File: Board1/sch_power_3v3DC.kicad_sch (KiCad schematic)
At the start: 6 parts, among them U2 TLV76133DCY

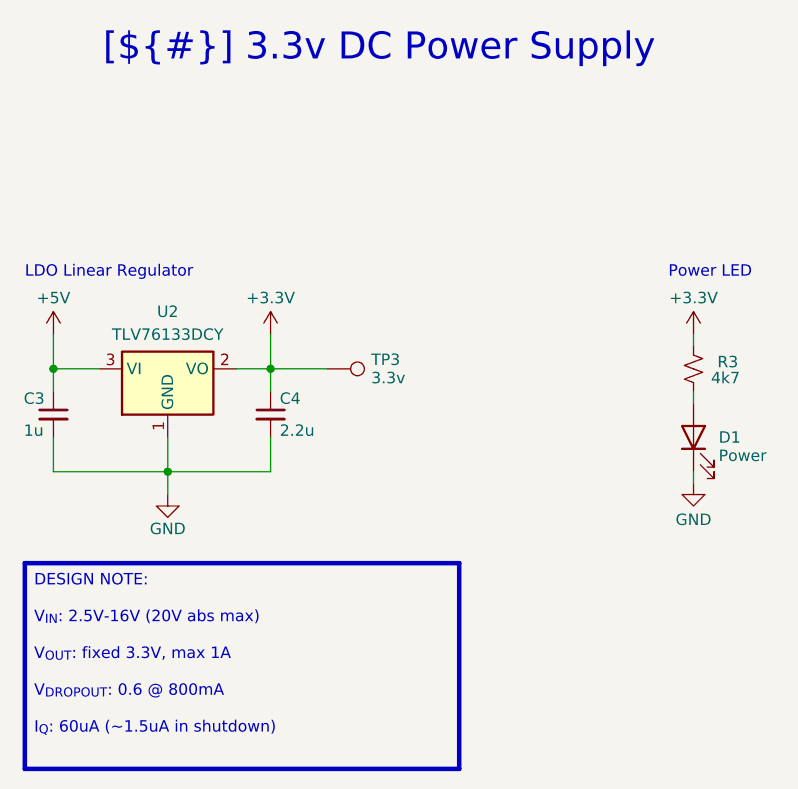
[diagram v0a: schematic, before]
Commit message: Resolve library and ERC issues
No changes to design.
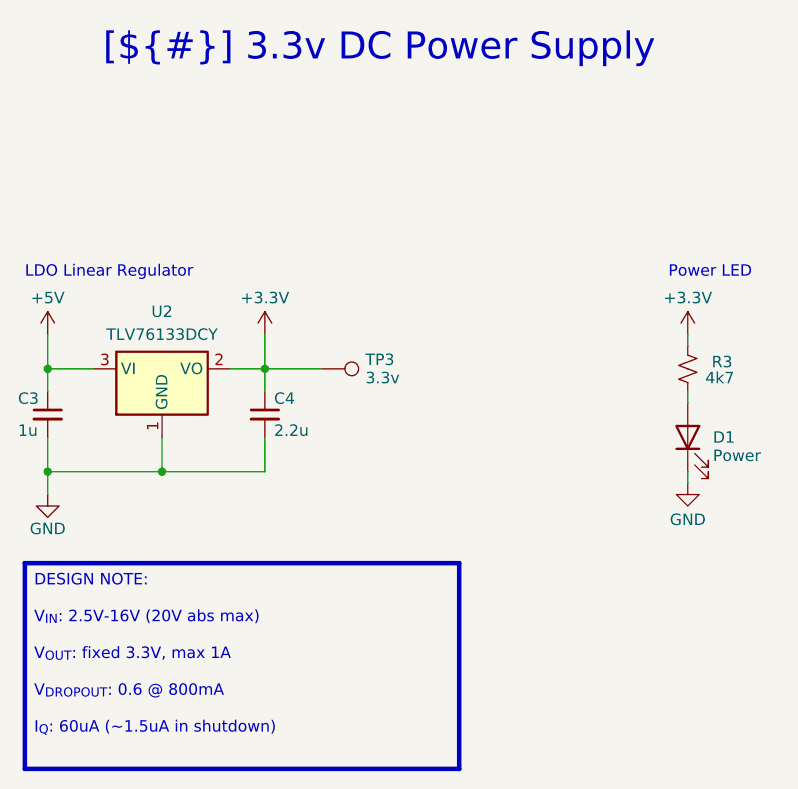
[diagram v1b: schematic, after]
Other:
- moved on the sheet: C3, C4, D1, R3, TP3, U2

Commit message: v1.2 release of board with bug fixes etc
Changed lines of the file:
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@@
 (kicad_sch
-	(version 20231120)
+	(version 20250114)
 	(generator "eeschema")
-	(generator_version "8.0")
+	(generator_version "9.0")
 	(paper "A4")
 	(title_block
 		(title "3.3v DC Power Supply")
-		(date "2025-02-19")
-		(rev "1.1")
+		(date "2025-03-08")
+		(rev "1.2")
 		(company "Wattle Labs")
 	)
-	(junction
-		(at 124.46 66.04)
-		(diameter 0)
-		(color 0 0 0 0)
-	)
-	(junction
-		(at 135.89 54.61)
-		(diameter 0)
-		(color 0 0 0 0)
-	)
-	(junction
-		(at 111.76 54.61)
-		(diameter 0)
-		(color 0 0 0 0)
-	)
-	(junction
-		(at 111.76 66.04)
-		(diameter 0)
-		(color 0 0 0 0)
-	)
-	(wire
-		(pts
-			(xy 124.46 66.04) (xy 135.89 66.04)
-		)
-		(stroke
-			(width 0)
-			(type default)
-		)
-	)
-	(wire
-		(pts
-			(xy 182.88 57.15) (xy 182.88 58.42)
-		)
-		(stroke
-			(width 0)
-			(type default)
-		)
-	)
-	(wire
-		(pts
-			(xy 124.46 66.04) (xy 124.46 62.23)
-		)
-		(stroke
-			(width 0)
-			(type default)
-		)
-	)
-	(wire
-		(pts
-			(xy 135.89 54.61) (xy 132.08 54.61)
-		)
-		(stroke
-			(width 0)
-			(type default)
-		)
-	)
-	(wire
-		(pts
-			(xy 111.76 50.8) (xy 111.76 54.61)
-		)
-		(stroke
-			(width 0)
-			(type default)
-		)
-	)
-	(wire
-		(pts
-			(xy 135.89 54.61) (xy 135.89 57.15)
-		)
-		(stroke
-			(width 0)
-			(type default)
-		)
-	)
-	(wire
-		(pts
-			(xy 182.88 50.8) (xy 182.88 52.07)
-		)
-		(stroke
-			(width 0)
-			(type default)
-		)
-	)
-	(wire
-		(pts
-			(xy 135.89 62.23) (xy 135.89 66.04)
-		)
-		(stroke
-			(width 0)
-			(type default)
-		)
-	)
-	(wire
-		(pts
-			(xy 111.76 54.61) (xy 116.84 54.61)
-		)
-		(stroke
-			(width 0)
-			(type default)
-		)
-	)
-	(wire
-		(pts
-			(xy 135.89 54.61) (xy 142.24 54.61)
-		)
-		(stroke
-			(width 0)
-			(type default)
-		)
-	)
-	(wire
-		(pts
-			(xy 111.76 66.04) (xy 124.46 66.04)
-		)
-		(stroke
-			(width 0)
-			(type default)
-		)
-	)
-	(wire
-		(pts
-			(xy 182.88 66.04) (xy 182.88 67.31)
-		)
-		(stroke
-			(width 0)
-			(type default)
-		)
-	)
-	(wire
-		(pts
-			(xy 135.89 50.8) (xy 135.89 54.61)
-		)
-		(stroke
-			(width 0)
-			(type default)
-		)
-	)
-	(wire
-		(pts
-			(xy 111.76 62.23) (xy 111.76 66.04)
-		)
-		(stroke
-			(width 0)
-			(type default)
-		)
-	)
-	(wire
-		(pts
-			(xy 111.76 66.04) (xy 111.76 68.58)
-		)
-		(stroke
-			(width 0)
-			(type default)
-		)
-	)
-	(wire
-		(pts
-			(xy 111.76 54.61) (xy 111.76 57.15)
-		)
-		(stroke
-			(width 0)
-			(type default)
+	(text "LDO Linear Regulator"
+		(exclude_from_sim no)
+		(at 109.22 43.18 0)
+		(effects
+			(font
+				(size 1.27 1.27)
+				(thickness 0.1588)
+			)
+			(justify left top)
+		)
+	)
+	(text "Power LED"
+		(exclude_from_sim no)
+		(at 180.721 43.18 0)
+		(effects
+			(font
+				(size 1.27 1.27)
+				(thickness 0.1588)
+			)
+			(justify left top)
 		)
 	)
@@
 		(at 109.22 76.2 0)
 		(size 48.26 22.86)
+		(margins 1.2025 1.2025 1.2025 1.2025)
 		(stroke
 			(width 0.5)
@@
 		(at 12.065 12.065 0)
 		(size 273.05 13.335)
+		(margins 2.2499 2.2499 2.2499 2.2499)
 		(stroke
 			(width -0.0001)
@@
 		)
 	)
-	(text "LDO Linear Regulator"
-		(exclude_from_sim no)
-		(at 109.22 43.18 0)
-		(effects
-			(font
-				(size 1.27 1.27)
-				(thickness 0.1588)
-			)
-			(justify left top)
-		)
-	)
-	(text "Power LED"
-		(exclude_from_sim no)
-		(at 180.721 43.18 0)
-		(effects
-			(font
-				(size 1.27 1.27)
-				(thickness 0.1588)
-			)
-			(justify left top)
-		)
-	)
+	(junction
+		(at 124.46 66.04)
+		(diameter 0)
+		(color 0 0 0 0)
+	)
+	(junction
+		(at 135.89 54.61)
+		(diameter 0)
+		(color 0 0 0 0)
+	)
+	(junction
+		(at 111.76 54.61)
+		(diameter 0)
+		(color 0 0 0 0)
+	)
+	(junction
+		(at 111.76 66.04)
+		(diameter 0)
+		(color 0 0 0 0)
+	)
+	(wire
+		(pts
+			(xy 124.46 66.04) (xy 135.89 66.04)
+		)
+		(stroke
+			(width 0)
+			(type default)
+		)
+	)
+	(wire
+		(pts
+			(xy 182.88 57.15) (xy 182.88 58.42)
+		)
+		(stroke
+			(width 0)
+			(type default)
+		)
+	)
+	(wire
+		(pts
+			(xy 124.46 66.04) (xy 124.46 62.23)
+		)
+		(stroke
+			(width 0)
+			(type default)
+		)
+	)
+	(wire
+		(pts
+			(xy 135.89 54.61) (xy 132.08 54.61)
+		)
+		(stroke
+			(width 0)
+			(type default)
+		)
+	)
+	(wire
+		(pts
+			(xy 111.76 50.8) (xy 111.76 54.61)
+		)
+		(stroke
+			(width 0)
+			(type default)
+		)
+	)
+	(wire
+		(pts
+			(xy 135.89 54.61) (xy 135.89 57.15)
+		)
+		(stroke
+			(width 0)
+			(type default)
+		)
+	)
+	(wire
+		(pts
+			(xy 182.88 50.8) (xy 182.88 52.07)
+		)
+		(stroke
+			(width 0)
+			(type default)
+		)
+	)
+	(wire
+		(pts
+			(xy 135.89 62.23) (xy 135.89 66.04)
+		)
+		(stroke
+			(width 0)
+			(type default)
+		)
+	)
+	(wire
+		(pts
+			(xy 111.76 54.61) (xy 116.84 54.61)
+		)
+		(stroke
+			(width 0)
+			(type default)
+		)
+	)
+	(wire
+		(pts
+			(xy 135.89 54.61) (xy 142.24 54.61)
+		)
+		(stroke
+			(width 0)
+			(type default)
+		)
+	)
+	(wire
+		(pts
+			(xy 111.76 66.04) (xy 124.46 66.04)
+		)
+		(stroke
+			(width 0)
+			(type default)
+		)
+	)
+	(wire
+		(pts
+			(xy 182.88 66.04) (xy 182.88 67.31)
+		)
+		(stroke
+			(width 0)
+			(type default)
+		)
+	)
+	(wire
+		(pts
+			(xy 135.89 50.8) (xy 135.89 54.61)
+		)
+		(stroke
+			(width 0)
+			(type default)
+		)
+	)
+	(wire
+		(pts
+			(xy 111.76 62.23) (xy 111.76 66.04)
+		)
+		(stroke
+			(width 0)
+			(type default)
+		)
+	)
+	(wire
+		(pts
+			(xy 111.76 66.04) (xy 111.76 68.58)
+		)
+		(stroke
+			(width 0)
+			(type default)
+		)
+	)
+	(wire
+		(pts
+			(xy 111.76 54.61) (xy 111.76 57.15)
+		)
+		(stroke
+			(width 0)
+			(type default)
+		)
+	)
